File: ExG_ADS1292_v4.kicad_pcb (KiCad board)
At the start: 2 copper layers, 32.2 x 21.7 mm, 68 parts, among them P1 CONN_2, P2 CONN_2, P3 CONN_2, P4 CONN_1, P5 CONN_01X04, Q1 DMP21D5UFB4-7B, U1 TPS63001, U2 ADS1291/2, U3 NRF528XX-QFAA, U4 MPU-9250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

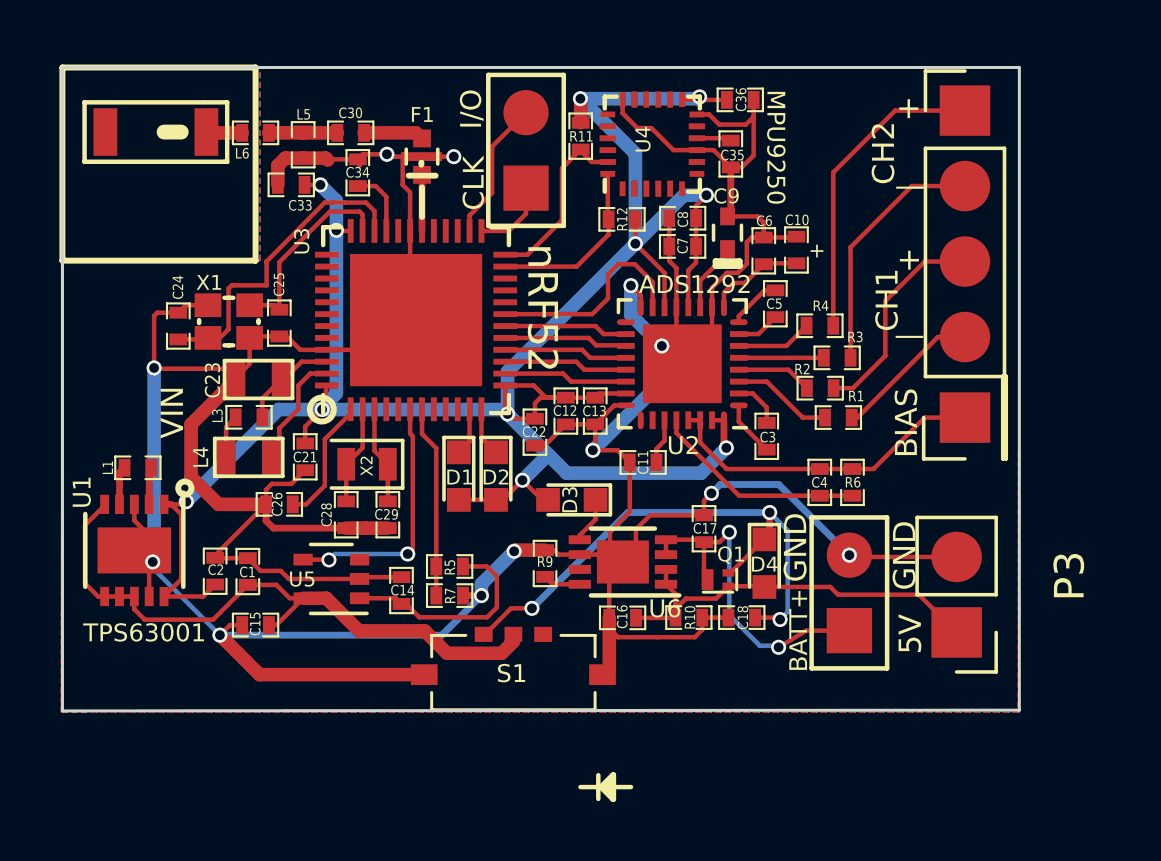
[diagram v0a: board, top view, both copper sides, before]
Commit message: Added TPS62746 1.8V regulator, replaced MPU9250 with ICM-20948, added SSAJ switch.
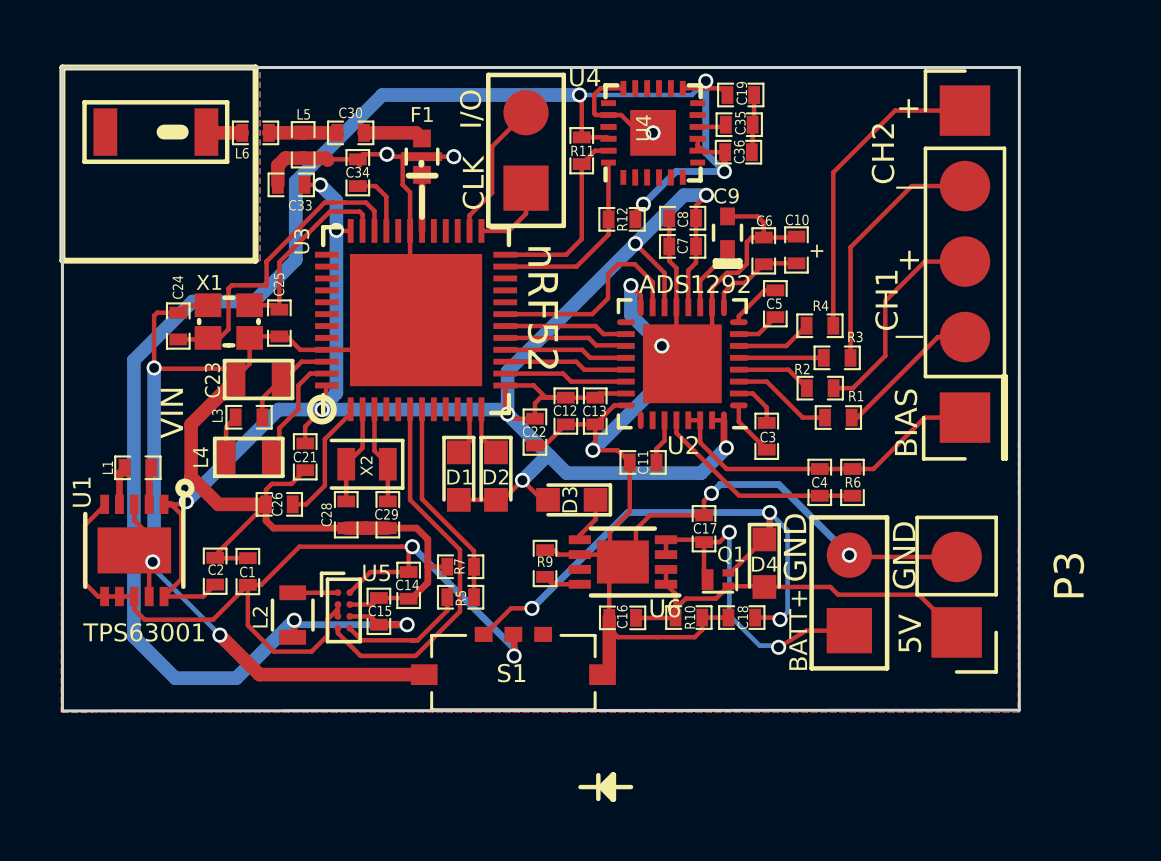
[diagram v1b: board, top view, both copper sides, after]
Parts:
- added C19: 100nF, SM0402, F.Cu at (288.7, 126.4)
- added L2: 2.2 uH, Resistors_SMD:R_0603, F.Cu at (273.6, 143.9)
- U4: value MPU-9250 -> ICM-20948; footprint Housings_DFN_QFN:QFN-24_3x3mm_Pitch0.4mm -> ICM_Custom:QFN-24_3x3mm_Pitch0.4mm
- U5: value TPS2294x -> TPS62746; footprint TO_SOT_Packages_SMD:SOT-353_SC-70-5 -> TPS62746:Texas_DSBGA-8_0.9x1.9mm_Layout2x4_P0.5mm
- moved C15 4.18 mm to (276.6, 143.8), turned to 90 degrees
- moved C36 1.76 mm to (288.6, 128.3)
- moved U5 1.14 mm to (275.4, 143.8), turned to 0 degrees
- moved R5 1.10 mm to (279.3, 143.3)
- moved R7 1.04 mm to (279.3, 142.3), turned to 0 degrees
- moved C35 1.03 mm to (288.7, 127.4), turned to 0 degrees
- moved R11 0.49 mm to (283.4, 128.3)
- moved U4 0.38 mm to (285.8, 127.7)
- moved C14 0.30 mm to (277.6, 142.9), turned to 270 degrees
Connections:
- C14 pad 1: Net-(C14-Pad1) -> VCC
- C15 pad 1: VCC -> 1.8V
- C36 pad 1: DVDD -> 1.8V
- R11 pad 1: DVDD -> 1.8V
- R12 pad 1: DVDD -> 1.8V
- R5 pad 1: /AIN_BAT_DIV_VOLTAGE -> Net-(R5-Pad1)
- R5 pad 2: Net-(C14-Pad1) -> /AIN_BAT_DIV_VOLTAGE
- U4 pad 12: DGND -> Net-(U4-Pad12)
- U4 pad 13: DVDD -> 1.8V
- U4 pad 20: Net-(U4-Pad20) -> DGND
- U4 pad 22: Net-(U4-Pad22) -> 1.8V
- U4 pad 8: Net-(U4-Pad8) -> 1.8V
- U4 pad 9: DGND -> 1.8V
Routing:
- net 1.8V: track 0.00 -> 60.8 mm, vias 0 -> 6
- net DGND: track 173.3 -> 154.9 mm, vias 12 -> 11
- net DVDD: track 82.4 -> 69.6 mm, vias 11 -> 9
- net VCC: track 21.6 -> 30.9 mm, vias 0 -> 2
- net Net-(C14-Pad1): track 7.34 -> 0.00 mm
- net Net-(R5-Pad1): track 0.00 -> 4.51 mm
- net /LOAD_SW_CTRL: track 8.58 -> 12.7 mm, vias 2 -> 0
- net Net-(L2-Pad1): track 0.00 -> 1.52 mm
- net /AIN_BAT_DIV_VOLTAGE: track 6.47 -> 7.05 mm
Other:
- board text added: "U4"
- board text added: "nRF52-ADS1292-ICM20948 ExG Prototype - 06/09/19 Yeo GaTech BNE Lab"
- board text removed: "MPU9250"
- board text removed: "nRF52-ADS1292-MPU ExG Prototype - 06/08/18 Yeo GaTech BNE Lab"
